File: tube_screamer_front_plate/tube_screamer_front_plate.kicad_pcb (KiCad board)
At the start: 2 copper layers, 80 x 100 mm, 15 parts

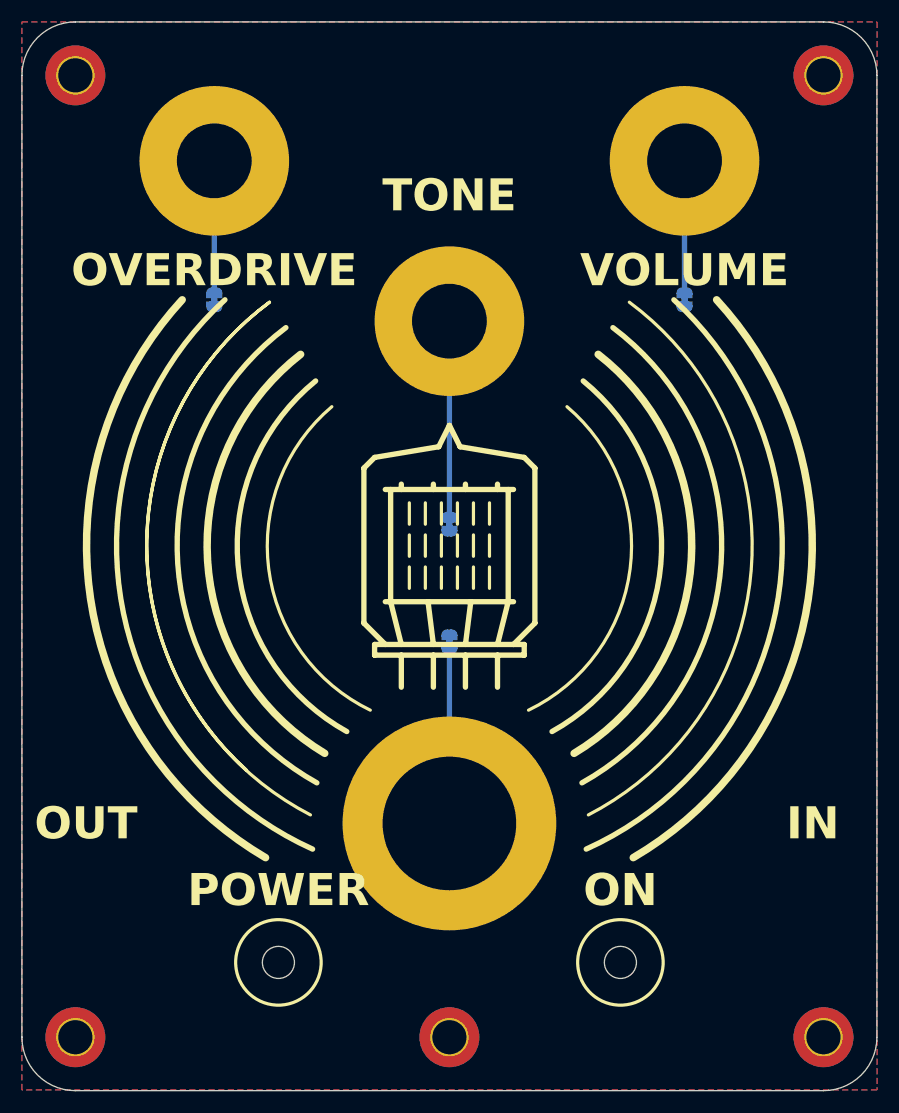
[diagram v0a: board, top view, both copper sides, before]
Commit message: Top plate update.
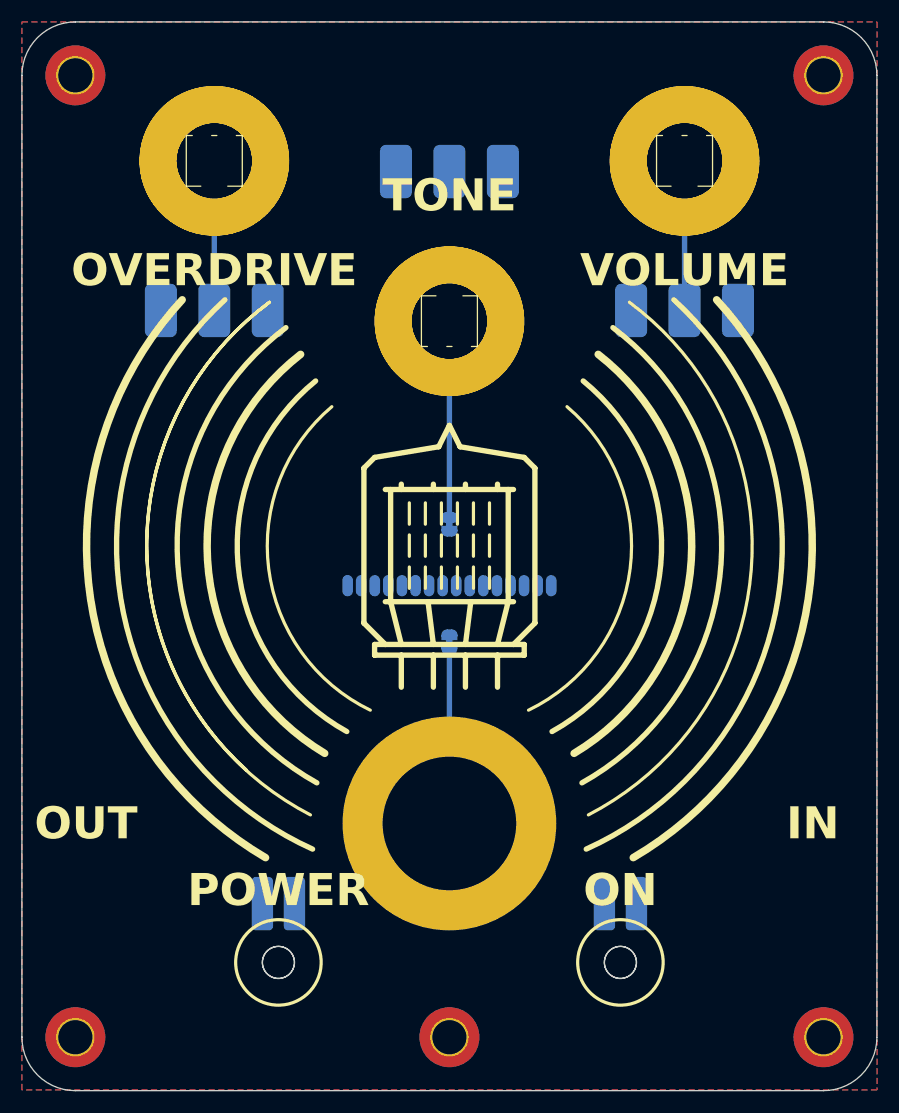
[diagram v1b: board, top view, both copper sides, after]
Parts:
- added D1: LED, pedale:red_led, F.Cu at (74.0, 138.0)
- added D2: LED, pedale:green_led, F.Cu at (106.0, 138.0)
- added J1: top_panel_connector, pedale:bottom_connector, B.Cu at (80.5, 102.8)
- added RV1: R_Potentiometer, pedale:top_plate_pot, F.Cu at (68.0, 63.0)
- added RV2: R_Potentiometer, pedale:top_plate_pot, F.Cu at (112.0, 63.0)
- added RV3: R_Potentiometer, pedale:top_plate_pot, F.Cu at (90.0, 78.0)

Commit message: Update schematic.
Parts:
- removed H10, H9: MountingHole, MountingHole:MountingHole_3mm
- removed H5, H6, H7: MountingHole_Pad, pedale:plated_pot_hole
- removed JP1, JP2, JP3: SolderJumper_2_Bridged, Jumper:SolderJumper-2_P1.3mm_Bridged_RoundedPad1.0x1.5mm
- moved JP4 29.2 mm to (90.0, 137.2), turned to 90 degrees
- moved J1 0.35 mm to (80.5, 102.4)
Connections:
- J1 pad 1: unconnected-(J1F-VCC-Pad1) -> Net-(D1-A)
- J1 pad 10: Net-(D2-A) -> unconnected-(J1F-GND-Pad10)
- J1 pad 3: unconnected-(J1F-GND-Pad3) -> Net-(D2-A)
- J1 pad 8: Net-(D1-A) -> unconnected-(J1F-VCC-Pad8)
- RV2 pad 1: Net-(J1B-Pin_5) -> Net-(J1B-Pin_9)
- RV2 pad 3: Net-(J1B-Pin_9) -> Net-(J1B-Pin_5)
- RV3 pad 1: Net-(J1C-Pin_12) -> Net-(J1C-Pin_16)
- RV3 pad 3: Net-(J1C-Pin_16) -> Net-(J1C-Pin_12)
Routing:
- net Net-(J1B-Pin_7): track 0.00 -> 64.5 mm
- net Net-(J1B-Pin_5): track 0.00 -> 62.0 mm
- net Net-(J1C-Pin_12): track 0.00 -> 47.5 mm
- net Net-(J1A-Pin_4): track 0.00 -> 44.8 mm
- net Net-(J1C-Pin_14): track 0.00 -> 43.1 mm
- net Net-(J1C-Pin_16): track 0.00 -> 43.0 mm
- net Net-(D2-A): track 0.00 -> 42.5 mm
- net Net-(J1B-Pin_9): track 0.00 -> 42.1 mm
- net Net-(J1A-Pin_2): track 0.00 -> 33.5 mm
- net Net-(D1-A): track 0.00 -> 33.2 mm
- net Net-(J1A-Pin_6): track 0.00 -> 31.5 mm
- net Net-(JP2-B): track 18.3 -> 0.00 mm
- net Net-(JP3-B): track 12.3 -> 0.00 mm
- net Net-(JP1-B): track 12.3 -> 0.00 mm
- net Net-(JP4-B): track 16.3 -> 11.8 mm

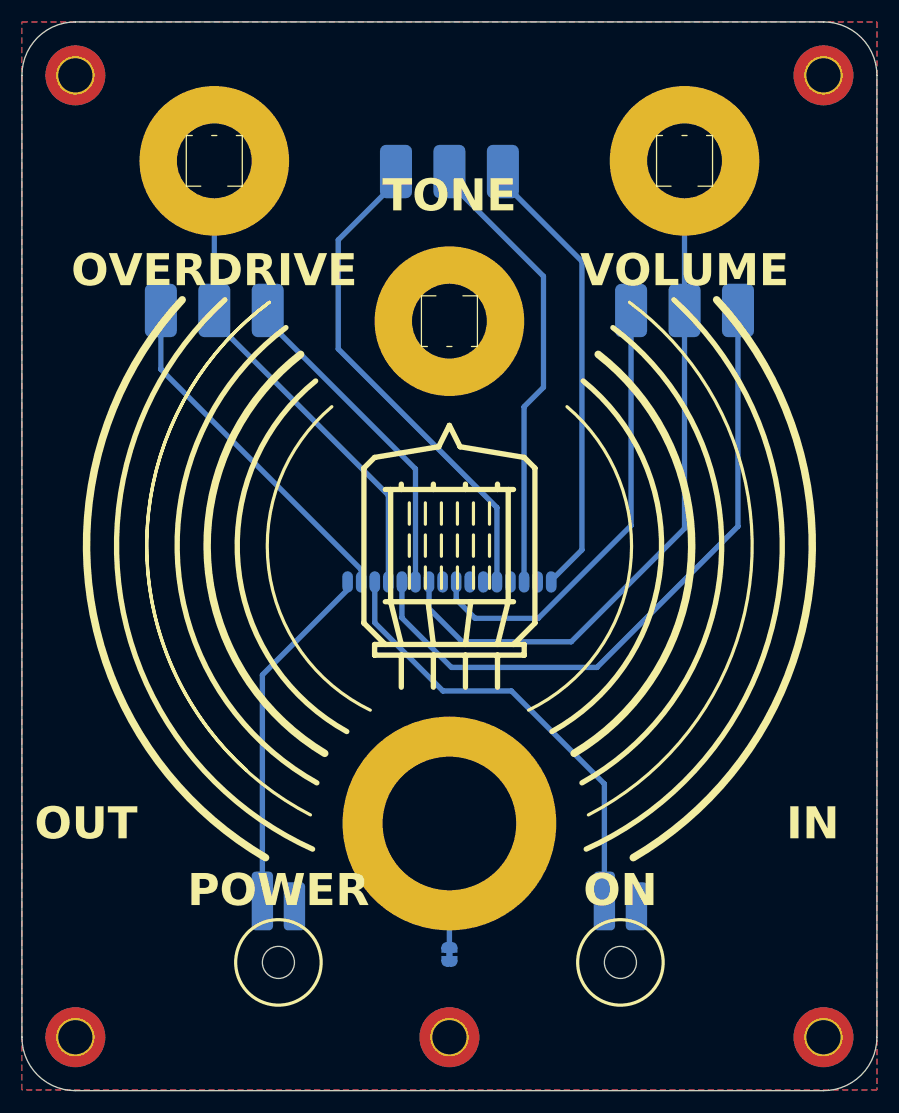
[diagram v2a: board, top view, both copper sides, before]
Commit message: 1 Red, 3 green connector.
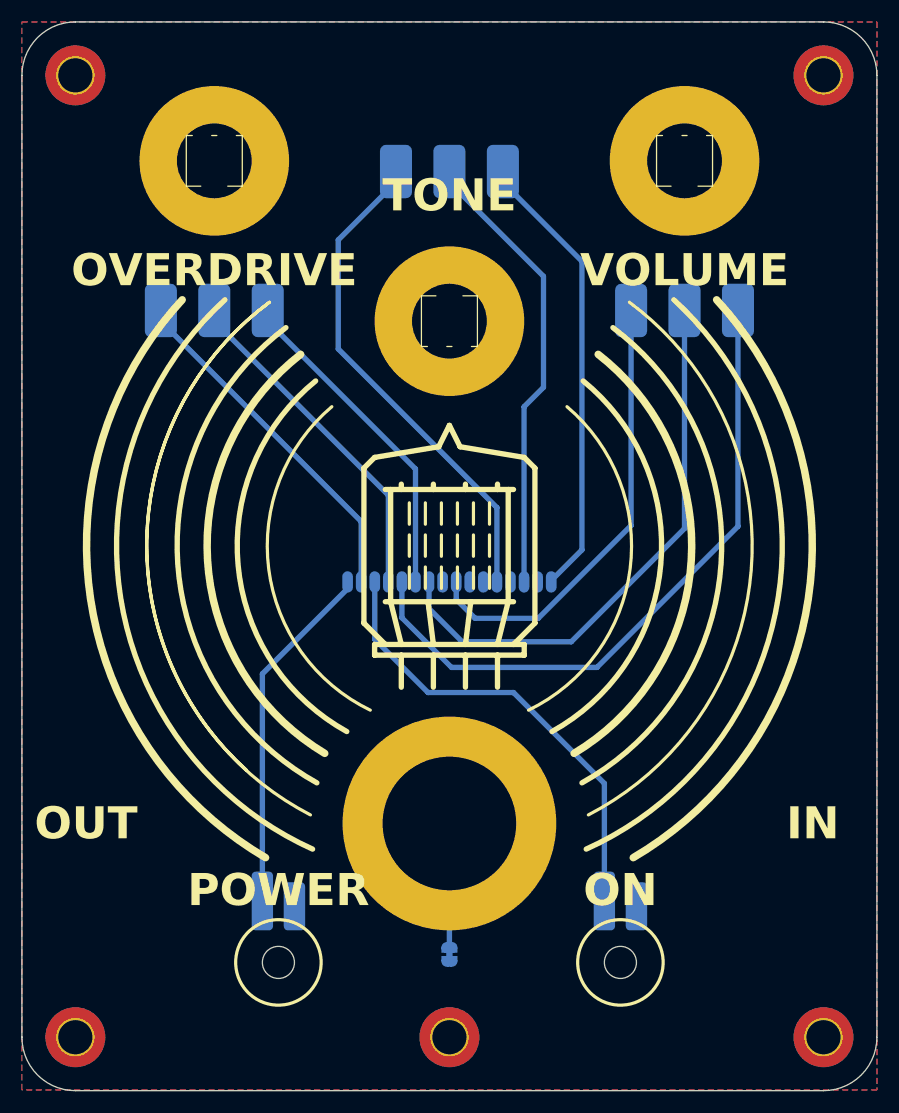
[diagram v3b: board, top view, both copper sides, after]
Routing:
- net Net-(J1B-Pin_7): track 64.5 -> 52.1 mm
- net Net-(J1A-Pin_4): track 44.8 -> 32.5 mm
- net Net-(D2-A): track 42.5 -> 43.4 mm
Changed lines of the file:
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@@
 			)
 		)
-		(property "Description" ""
+		(property "Description" "Mounting Hole without connection"
 			(at 0 0 0)
 			(unlocked yes)
@@
 			)
 		)
-		(property "Description" ""
+		(property "Description" "Mounting Hole without connection"
 			(at 0 0 0)
 			(unlocked yes)
@@
 			)
 		)
-		(property "Description" ""
+		(property "Description" "Mounting Hole without connection"
 			(at 0 0 0)
 			(unlocked yes)
@@
 			)
 		)
-		(property "Description" ""
+		(property "Description" "Mounting Hole without connection"
 			(at 0 0 0)
 			(unlocked yes)
@@
 			)
 		)
-		(property "Description" ""
+		(property "Description" "Mounting Hole without connection"
 			(at 0 0 0)
 			(unlocked yes)
@@
 			(layers "B.Cu" "B.Mask" "B.Paste")
 			(net 6 "Net-(D2-A)")
-			(pinfunction "Pin_10")
+			(pinfunction "1")
 			(pintype "passive")
 		)
@@
 	)
 	(segment
-		(start 72.5 111.1)
+		(start 72.5 111)
 		(end 72.5 132.25)
 		(width 0.5)
@@
 	)
 	(segment
-		(start 80.475 102.4)
-		(end 80.475 103.125)
+		(start 80.475 103.025)
+		(end 72.5 111)
 		(width 0.5)
 		(layer "B.Cu")
@@
 	)
 	(segment
-		(start 80.475 103.125)
-		(end 72.5 111.1)
+		(start 80.475 102.4)
+		(end 80.475 103.025)
 		(width 0.5)
 		(layer "B.Cu")
@@
 	)
 	(segment
-		(start 104.5 121.3)
-		(end 104.5 132.25)
+		(start 83.015 102.4)
+		(end 83.015 107.765)
 		(width 0.5)
 		(layer "B.Cu")
@@
 	)
 	(segment
-		(start 83.015 102.4)
-		(end 83.015 106.215)
+		(start 104.5 121.25)
+		(end 104.5 132.25)
 		(width 0.5)
 		(layer "B.Cu")
@@
 	)
 	(segment
-		(start 95.8 112.6)
-		(end 104.5 121.3)
+		(start 88 112.75)
+		(end 96 112.75)
 		(width 0.5)
 		(layer "B.Cu")
@@
 	)
 	(segment
-		(start 89.4 112.6)
-		(end 95.8 112.6)
+		(start 83.015 107.765)
+		(end 88 112.75)
 		(width 0.5)
 		(layer "B.Cu")
@@
 	)
 	(segment
-		(start 83.015 106.215)
-		(end 89.4 112.6)
+		(start 96 112.75)
+		(end 104.5 121.25)
 		(width 0.5)
 		(layer "B.Cu")
@@
 	)
 	(segment
-		(start 68 75.35)
-		(end 68 63)
-		(width 0.5)
-		(layer "B.Cu")
-		(net 10)
-	)
-	(segment
 		(start 84.285 102.75)
 		(end 84.285 94.285)
@@
 	)
 	(segment
-		(start 112 75.35)
-		(end 112 63)
-		(width 0.5)
-		(layer "B.Cu")
-		(net 15)
-	)
-	(segment
 		(start 88.095 102.75)
 		(end 88.095 104.895)
@@
 	)
 	(segment
-		(start 81.745 101.25)
-		(end 63 82.505)
+		(start 81.745 96.745)
+		(end 63 78)
 		(width 0.5)
 		(layer "B.Cu")
@@
 	)
 	(segment
-		(start 81.745 102.75)
-		(end 81.745 101.25)
+		(start 63 78)
+		(end 63 77)
 		(width 0.5)
 		(layer "B.Cu")
@@
 	)
 	(segment
-		(start 63 82.505)
-		(end 63 77)
+		(start 81.745 102.75)
+		(end 81.745 96.745)
 		(width 0.5)
 		(layer "B.Cu")

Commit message: Pots checked, all good.
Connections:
- J1 pad 1: Net-(D1-A) -> unconnected-(J1F-VCC-Pad1)
- J1 pad 10: unconnected-(J1F-GND-Pad10) -> Net-(D2-A)
- J1 pad 3: Net-(D2-A) -> unconnected-(J1F-GND-Pad3)
- J1 pad 8: unconnected-(J1F-VCC-Pad8) -> Net-(D1-A)
- RV1 pad 1: Net-(J1A-Pin_2) -> Net-(J1A-Pin_6)
- RV1 pad 3: Net-(J1A-Pin_6) -> Net-(J1A-Pin_2)
- RV2 pad 1: Net-(J1B-Pin_9) -> Net-(J1C-Pin_16)
- RV2 pad 2: Net-(J1B-Pin_7) -> Net-(J1C-Pin_14)
- RV2 pad 3: Net-(J1B-Pin_5) -> Net-(J1C-Pin_12)
- RV3 pad 1: Net-(J1C-Pin_16) -> Net-(J1B-Pin_9)
- RV3 pad 2: Net-(J1C-Pin_14) -> Net-(J1B-Pin_7)
- RV3 pad 3: Net-(J1C-Pin_12) -> Net-(J1B-Pin_5)
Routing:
- net Net-(J1A-Pin_6): track 31.5 -> 54.6 mm
- net Net-(J1B-Pin_5): track 62.0 -> 41.7 mm
- net Net-(J1A-Pin_2): track 33.5 -> 45.5 mm
- net Net-(J1C-Pin_14): track 43.1 -> 31.6 mm
- net Net-(D2-A): track 43.4 -> 35.1 mm
- net Net-(J1B-Pin_7): track 52.1 -> 46.4 mm
- net Net-(D1-A): track 33.2 -> 36.8 mm
- net Net-(J1B-Pin_9): track 42.1 -> 45.6 mm
- net Net-(J1C-Pin_12): track 47.5 -> 50.9 mm
- net Net-(J1C-Pin_16): track 43.0 -> 44.1 mm

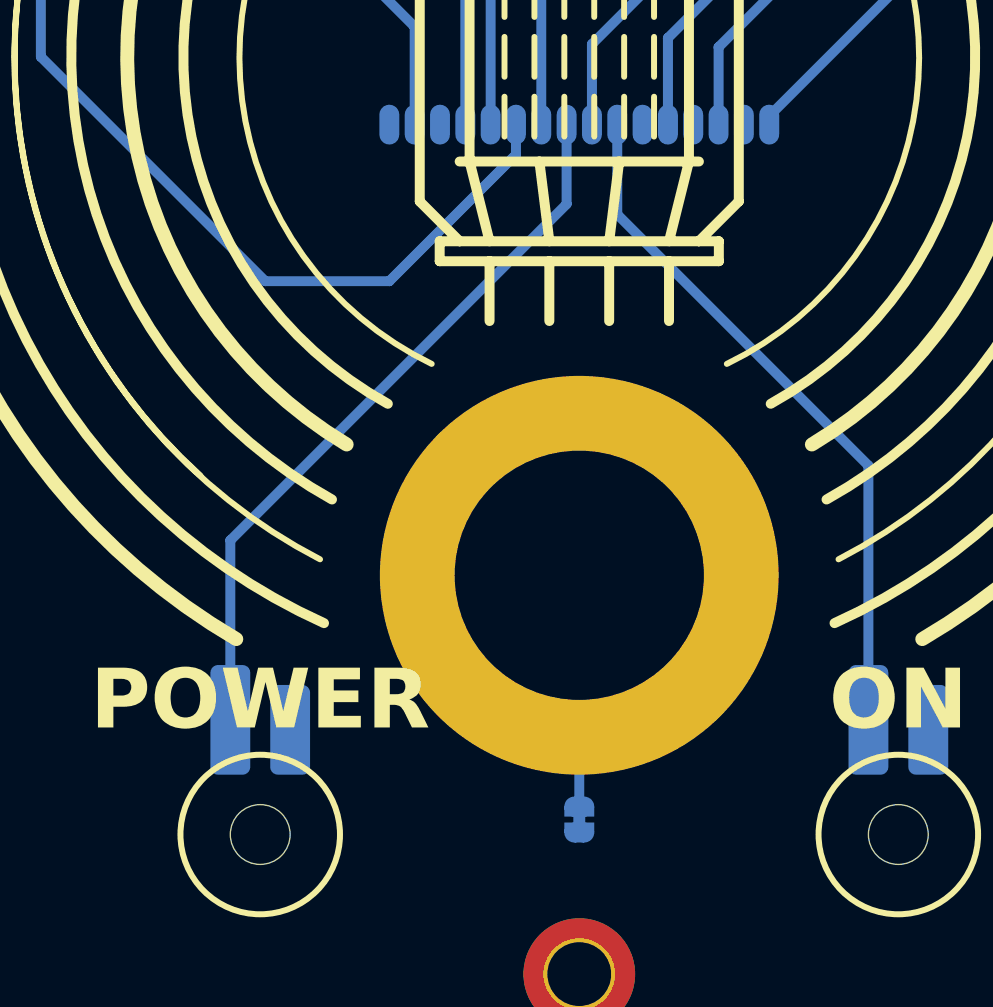
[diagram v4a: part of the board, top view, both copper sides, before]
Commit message: Fixed diodes on front plate, fixed power schem.
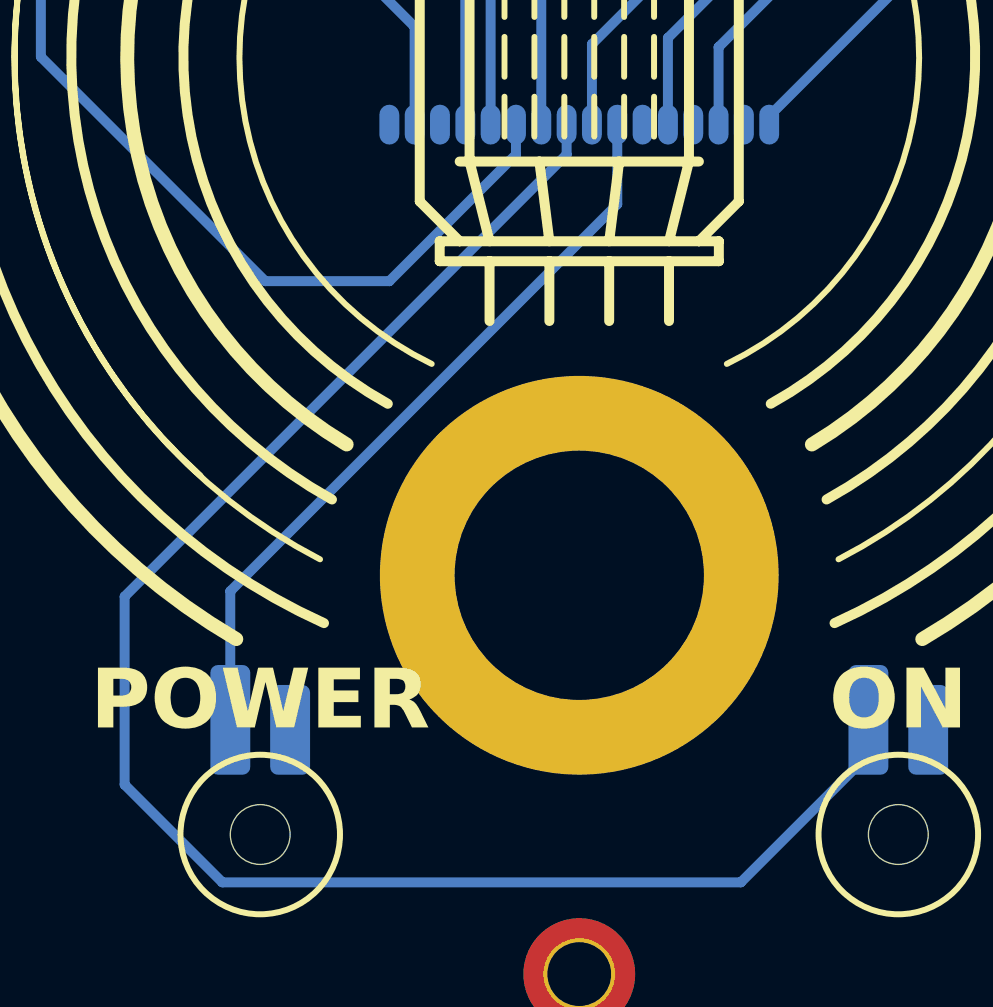
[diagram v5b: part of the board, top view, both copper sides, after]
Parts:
- removed JP4: SolderJumper_2_Bridged, Jumper:SolderJumper-2_P1.3mm_Bridged_RoundedPad1.0x1.5mm
- RV1, RV2, RV3: value R_Potentiometer -> pot_gnd
- moved D1 32.0 mm to (106.0, 138.0)
- moved D2 32.0 mm to (74.0, 138.0)
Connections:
- H8 pad 1: Net-(JP4-B) -> 0
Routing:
- net Net-(D1-A): track 36.8 -> 86.0 mm
- net Net-(JP4-B): track 11.8 -> 0.00 mm
- net Net-(D2-A): track 35.1 -> 37.9 mm
